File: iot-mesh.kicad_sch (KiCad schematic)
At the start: 18 parts, among them J1 DS18B20 connector, J2 BME280 connector, J5 Power Connector, U1 XIAO-nRF52840-DIP, U2 WEMOS_D1_mini, U3 L7805

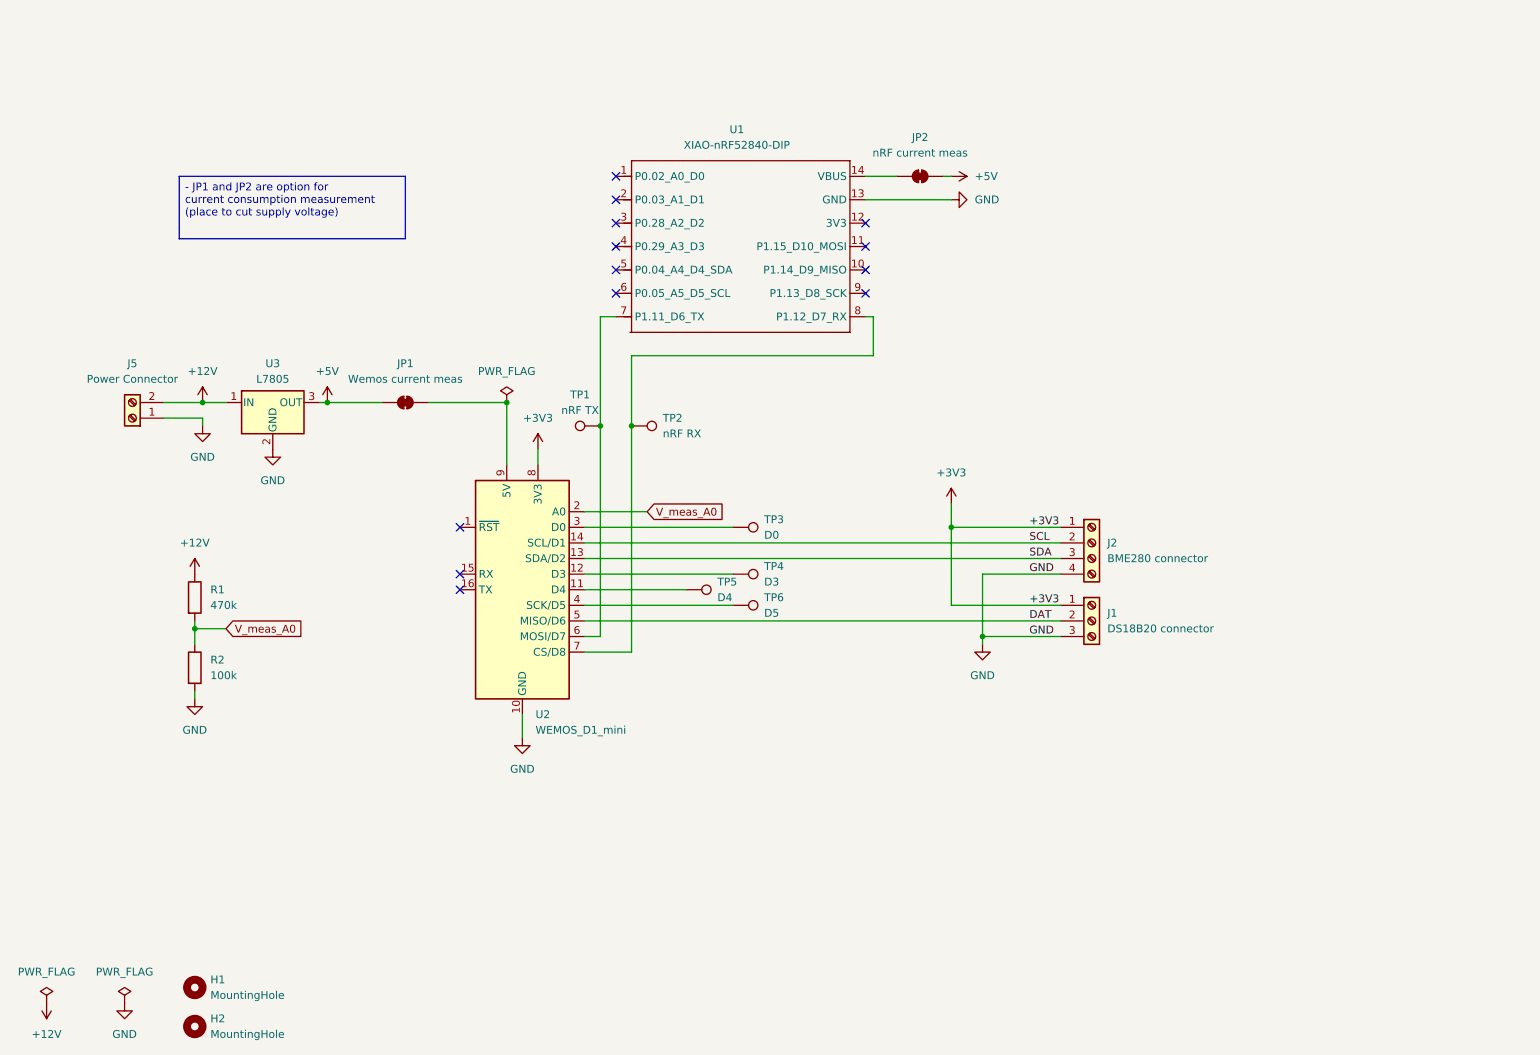
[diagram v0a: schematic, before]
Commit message: Add pin headers for nRF
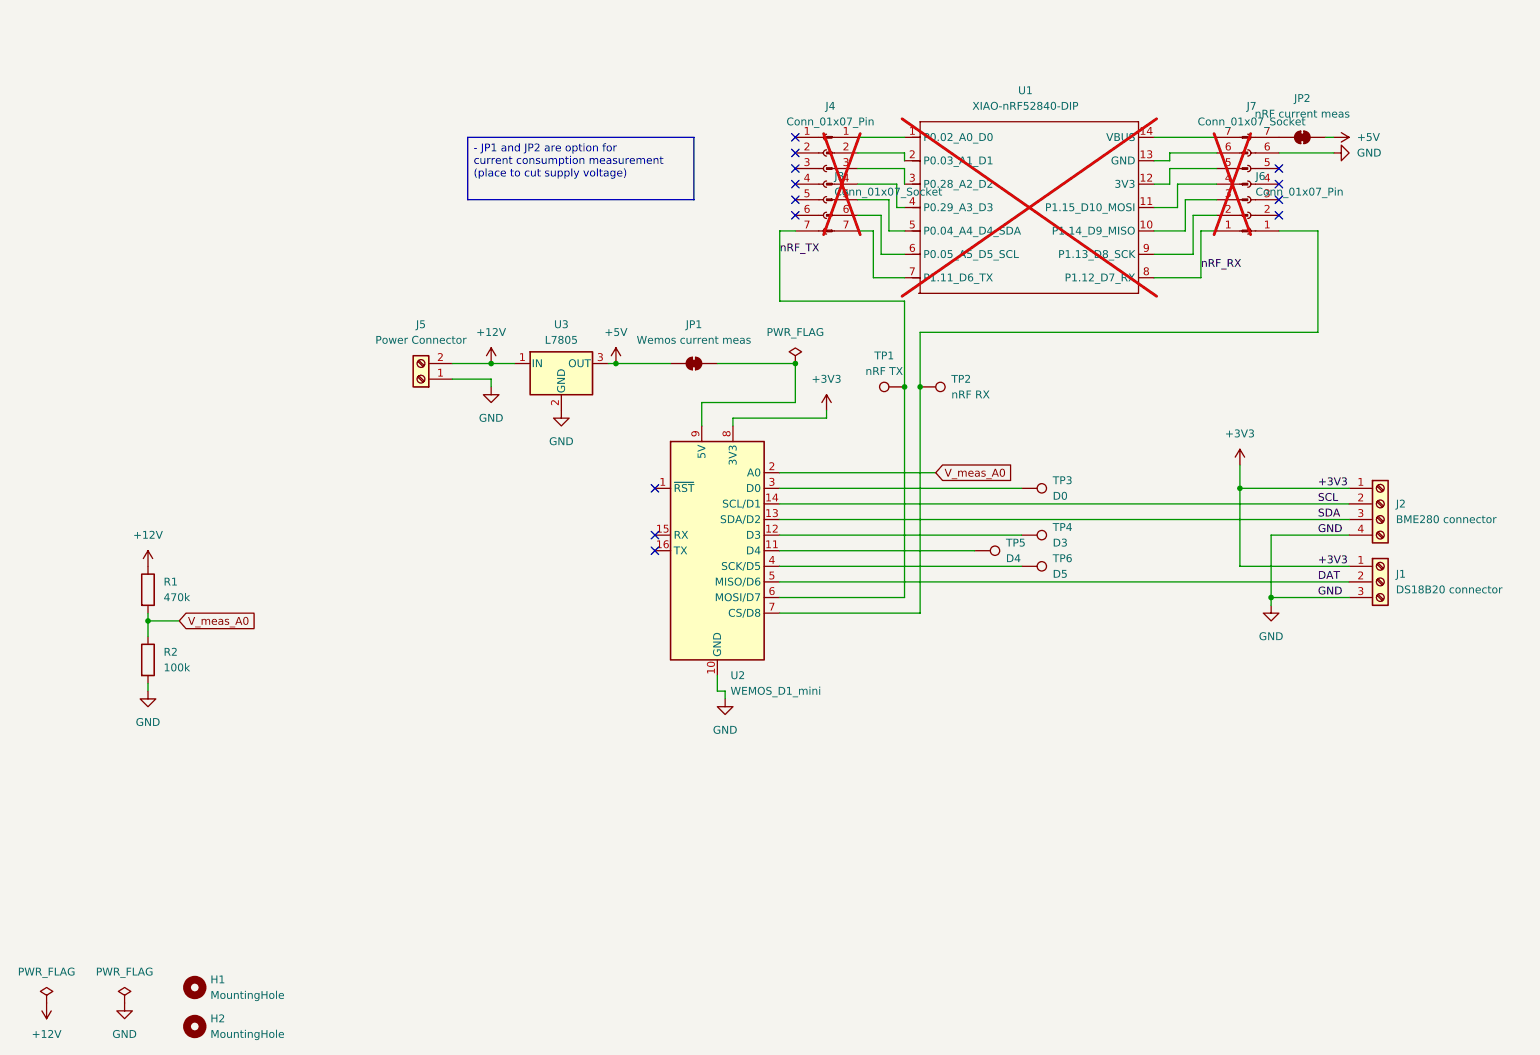
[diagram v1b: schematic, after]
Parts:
- added J3, J7: Conn_01x07_Socket, Connector_PinSocket_2.54mm:PinSocket_1x07_P2.54mm_Vertical, symbol Connector:Conn_01x07_Socket
- added J4, J6: Conn_01x07_Pin, Connector_PinHeader_2.54mm:PinHeader_1x07_P2.54mm_Vertical, symbol Connector:Conn_01x07_Pin
- U1: now not fitted
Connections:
- net GND: now also J7.6 (Pin_6); no longer U1.13 (GND)
- net at TP2.1, U2.7 (CS/D8): now also J7.1 (Pin_1); no longer U1.8 (P1.12_D7_RX)
- net nRF_TX: now reaches TP1.1, U2.6 (MOSI/D7)
- net nRF_TX: now also J3.7 (Pin_7); no longer U1.7 (P1.11_D6_TX)
- net at U1.1 (P0.02_A0_D0): now also J4.1 (Pin_1)
- net at U1.10 (P1.14_D9_MISO): now also J6.3 (Pin_3)
- net at U1.11 (P1.15_D10_MOSI): now also J6.4 (Pin_4)
- net at U1.12 (3V3): now also J6.5 (Pin_5)
- net at U1.14 (VBUS): now also J6.7 (Pin_7); no longer JP2.1 (A)
- net at U1.2 (P0.03_A1_D1): now also J4.2 (Pin_2)
- net at U1.3 (P0.28_A2_D2): now also J4.3 (Pin_3)
- net at U1.4 (P0.29_A3_D3): now also J4.4 (Pin_4)
- net at U1.5 (P0.04_A4_D4_SDA): now also J4.5 (Pin_5)
- net at U1.6 (P0.05_A5_D5_SCL): now also J4.6 (Pin_6)
- net at U1.9 (P1.13_D8_SCK): now also J6.2 (Pin_2)
- new net: J6.6 (Pin_6), U1.13 (GND)
- new net: J4.7 (Pin_7), U1.7 (P1.11_D6_TX)
- new net: J7.7 (Pin_7), JP2.1 (A)
- new net nRF_RX: J6.1 (Pin_1), U1.8 (P1.12_D7_RX)
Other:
- moved on the sheet: J1, J2, J5, JP1, JP2, R1, R2, TP1, TP2, TP3, TP4, TP5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

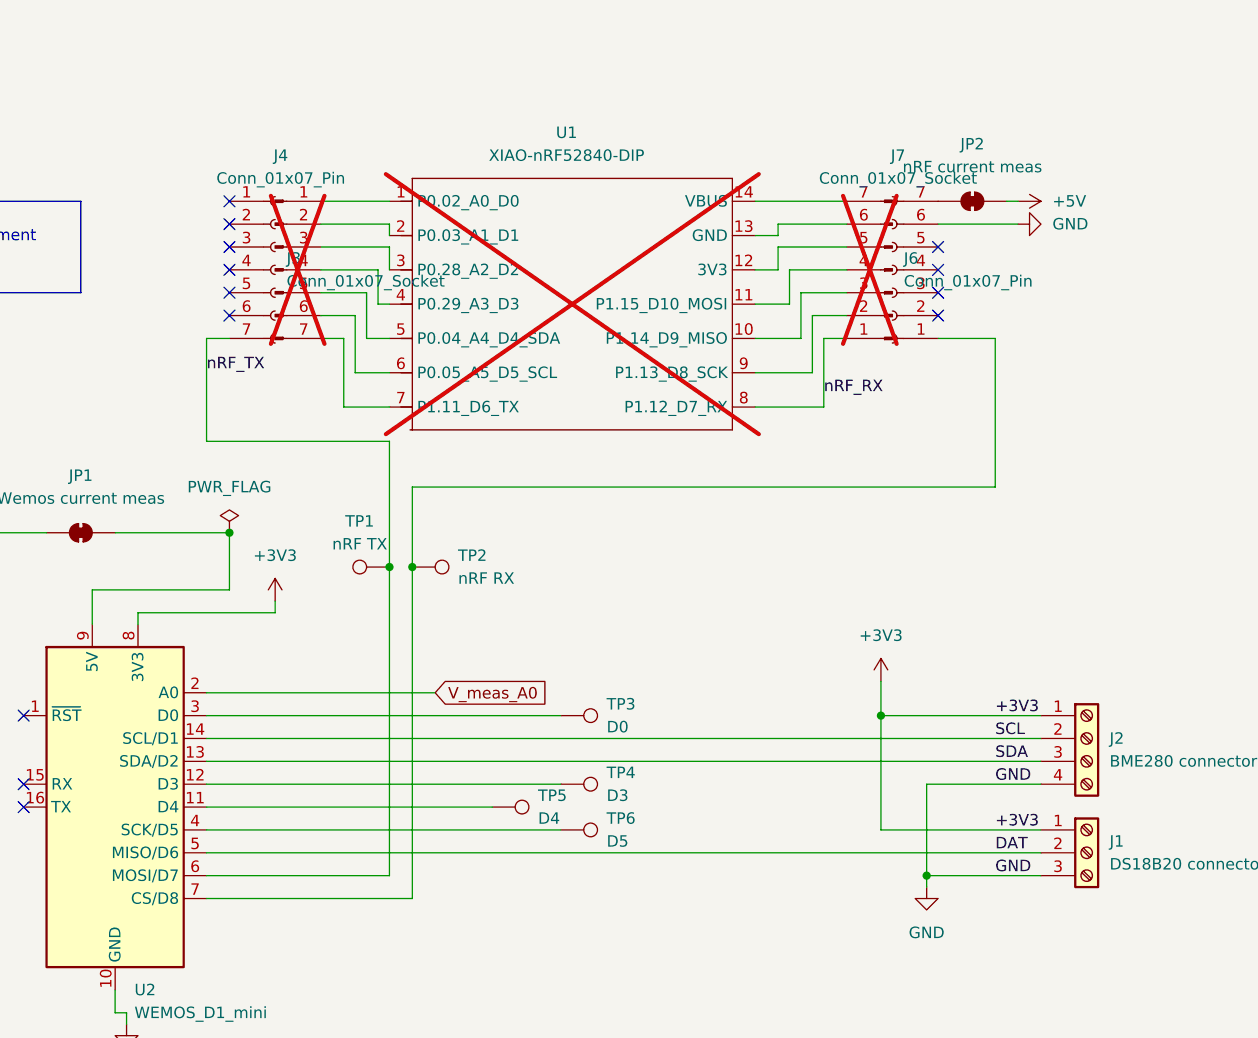
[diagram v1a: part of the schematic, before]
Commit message: 
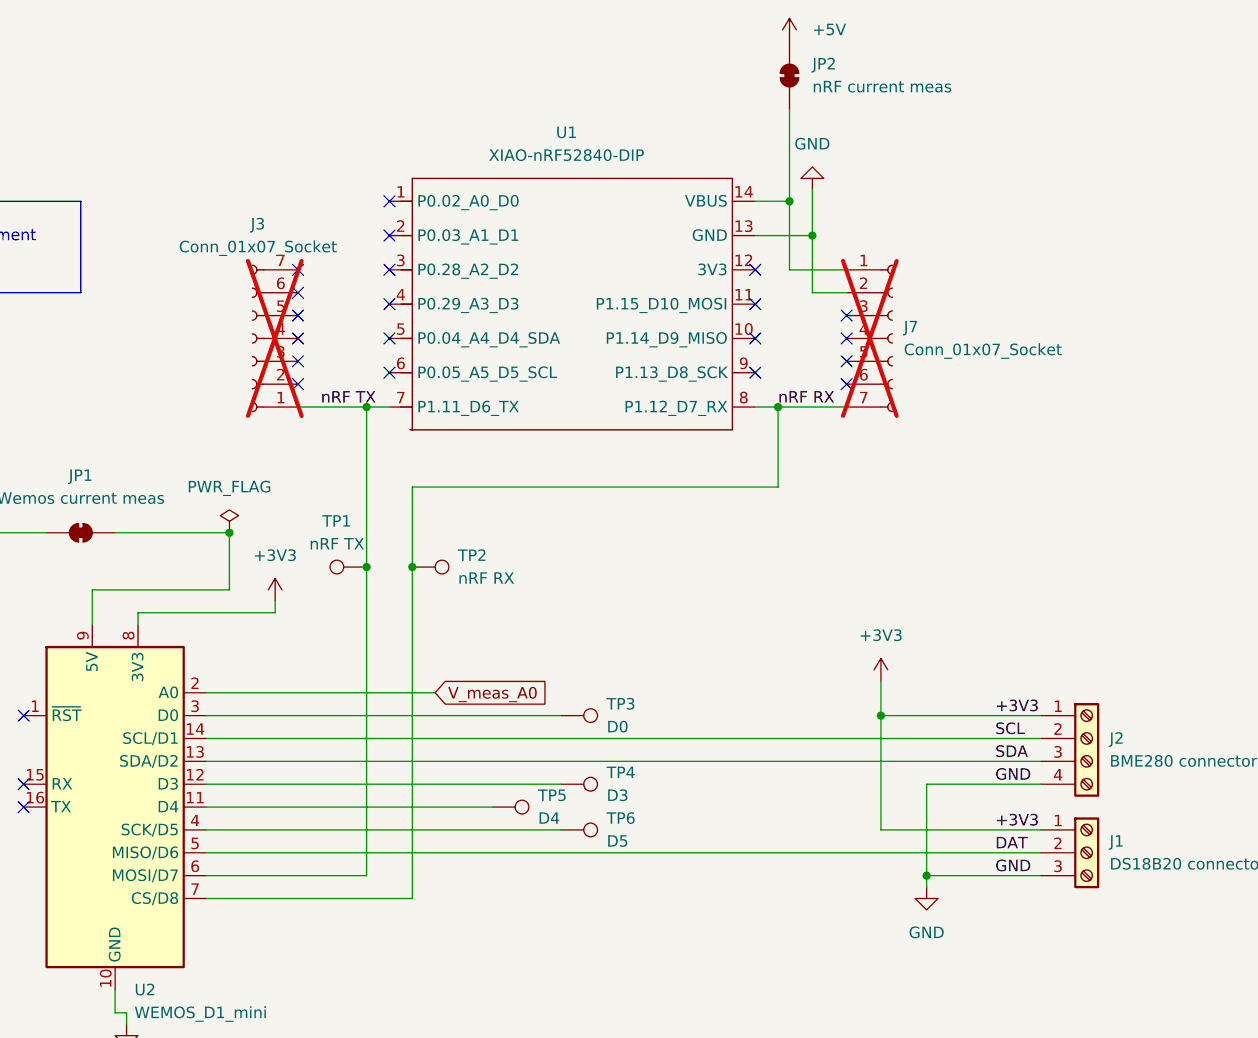
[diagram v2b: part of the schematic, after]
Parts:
- removed J4, J6: Conn_01x07_Pin, Connector_PinHeader_2.54mm:PinHeader_1x07_P2.54mm_Vertical, symbol Connector:Conn_01x07_Pin
- J3, J7: now not fitted
- U1: now fitted
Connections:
- net nRF_RX is gone; now on net nRF RX: U1.8 (P1.12_D7_RX)
- net GND: now also J7.2 (Pin_2), U1.13 (GND); no longer J7.6 (Pin_6)
- net at U1.14 (VBUS): now also J7.1 (Pin_1), JP2.1 (A)
- net nRF RX: now reaches TP2.1, U2.7 (CS/D8)
- net nRF RX: now also J7.7 (Pin_7); no longer J7.1 (Pin_1)
- net nRF TX: now reaches U1.7 (P1.11_D6_TX)
- net nRF TX: now also J3.1 (Pin_1), TP1.1, U2.6 (MOSI/D7)
- removed net nRF_TX: J3.7 (Pin_7), TP1.1, U2.6 (MOSI/D7)
- no-connect marks 13 -> 23
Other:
- moved on the sheet: JP2, TP1
